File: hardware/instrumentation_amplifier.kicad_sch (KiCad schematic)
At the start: 7 parts, among them U3 MCP6N11-010, U4 MCP4542

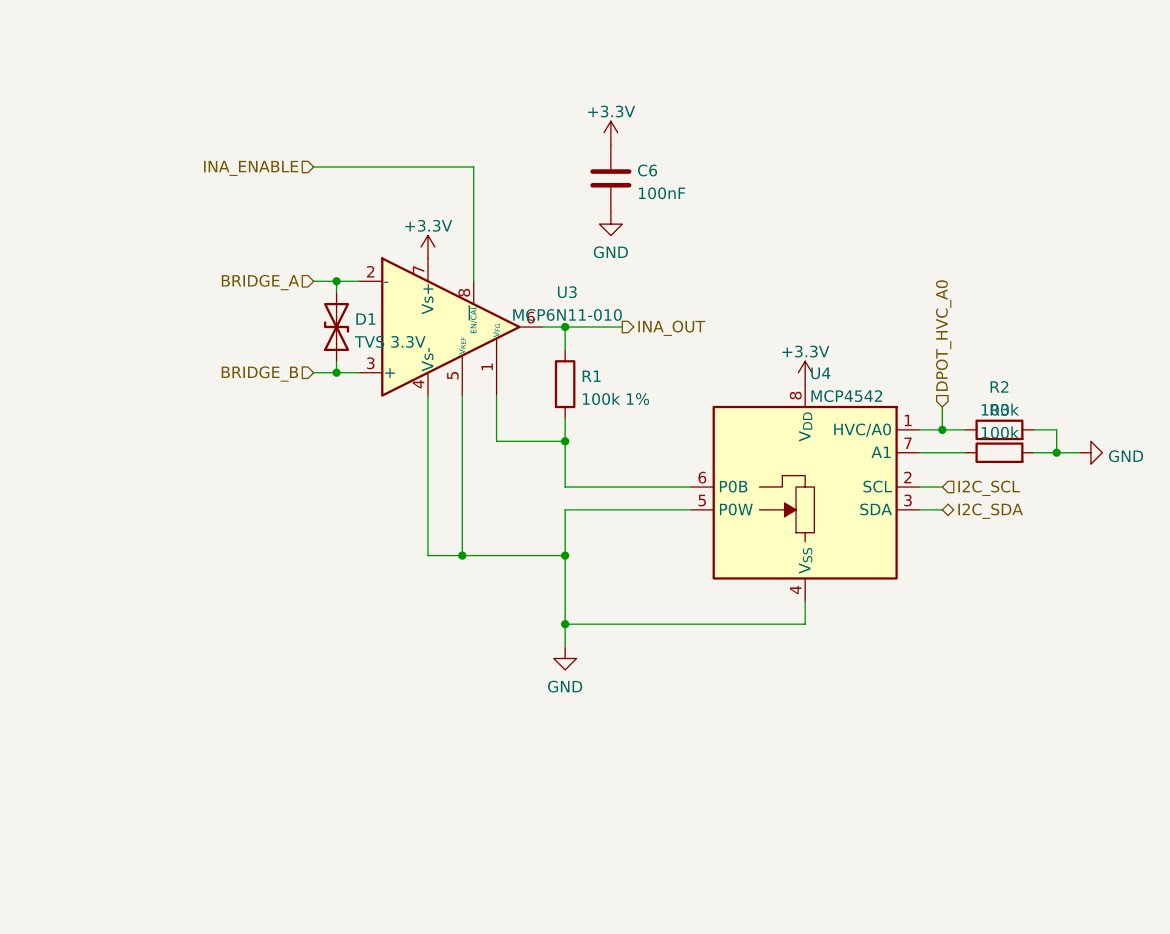
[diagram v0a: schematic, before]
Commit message: Updated schematic according to reference design
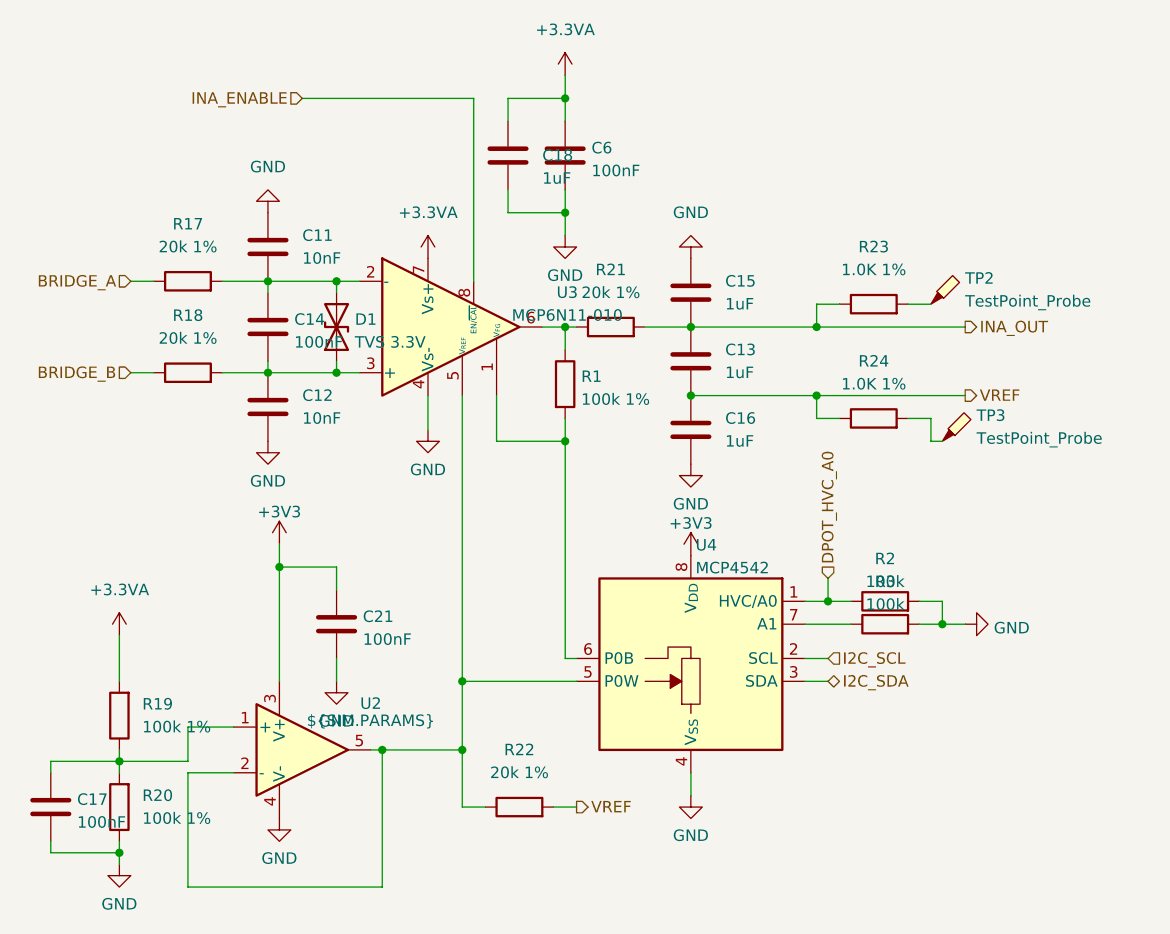
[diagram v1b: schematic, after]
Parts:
- added C11, C12: 10nF, Capacitor_SMD:C_0603_1608Metric_Pad1.08x0.95mm_HandSolder, symbol Device:C
- added C13, C15, C16, C18: 1uF, Capacitor_SMD:C_0603_1608Metric_Pad1.08x0.95mm_HandSolder, symbol Device:C
- added C14, C17, C21: 100nF, Capacitor_SMD:C_0603_1608Metric_Pad1.08x0.95mm_HandSolder, symbol Device:C
- added R17, R18, R21, R22: 20k 1%, Resistor_SMD:R_0603_1608Metric_Pad0.98x0.95mm_HandSolder, symbol Device:R
- added R19, R20: 100k 1%, Resistor_SMD:R_0603_1608Metric_Pad0.98x0.95mm_HandSolder, symbol Device:R
- added R23, R24: 1.0K 1%, Resistor_SMD:R_0603_1608Metric_Pad0.98x0.95mm_HandSolder, symbol Device:R
- added TP2, TP3: TestPoint_Probe, symbol Connector:TestPoint_Probe
- added U2: ${SIM.PARAMS}, symbol Simulation_SPICE:OPAMP
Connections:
- net +3V3: now also C21.1, U2.3 (V+); no longer C6.1, U3.7 (Vs+)
- net BRIDGE_A: now also R17.1; no longer D1.2 (A2), U3.2 (-)
- net BRIDGE_B: now also R18.1; no longer D1.1 (A1), U3.3 (+)
- net GND: now also C11.1, C12.2, C15.1, C16.2, C17.2, C18.2, C21.2, R20.1, U2.4 (V-); no longer U3.5 (V_{REF}), U4.5 (P0W)
- net INA_OUT: now also C13.1, C15.2, R21.2, R23.1; no longer R1.1, U3.6
- new net: R24.2, TP3.1
- new net: R1.1, R21.1, U3.6
- new net: C12.1, C14.2, D1.1 (A1), R18.2, U3.3 (+)
- new net: C17.1, R19.1, R20.2, U2.1 (+)
- new net: R22.1, U2.2 (-), U2.5, U3.5 (V_{REF}), U4.5 (P0W)
- new net: C11.2, C14.1, D1.2 (A2), R17.2, U3.2 (-)
- new net: R23.2, TP2.1
- new net +3.3VA: C18.1, C6.1, R19.2, U3.7 (Vs+)
- new net VREF: C13.2, C16.1, R22.2, R24.1
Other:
- moved on the sheet: C6, R2, R3, U4

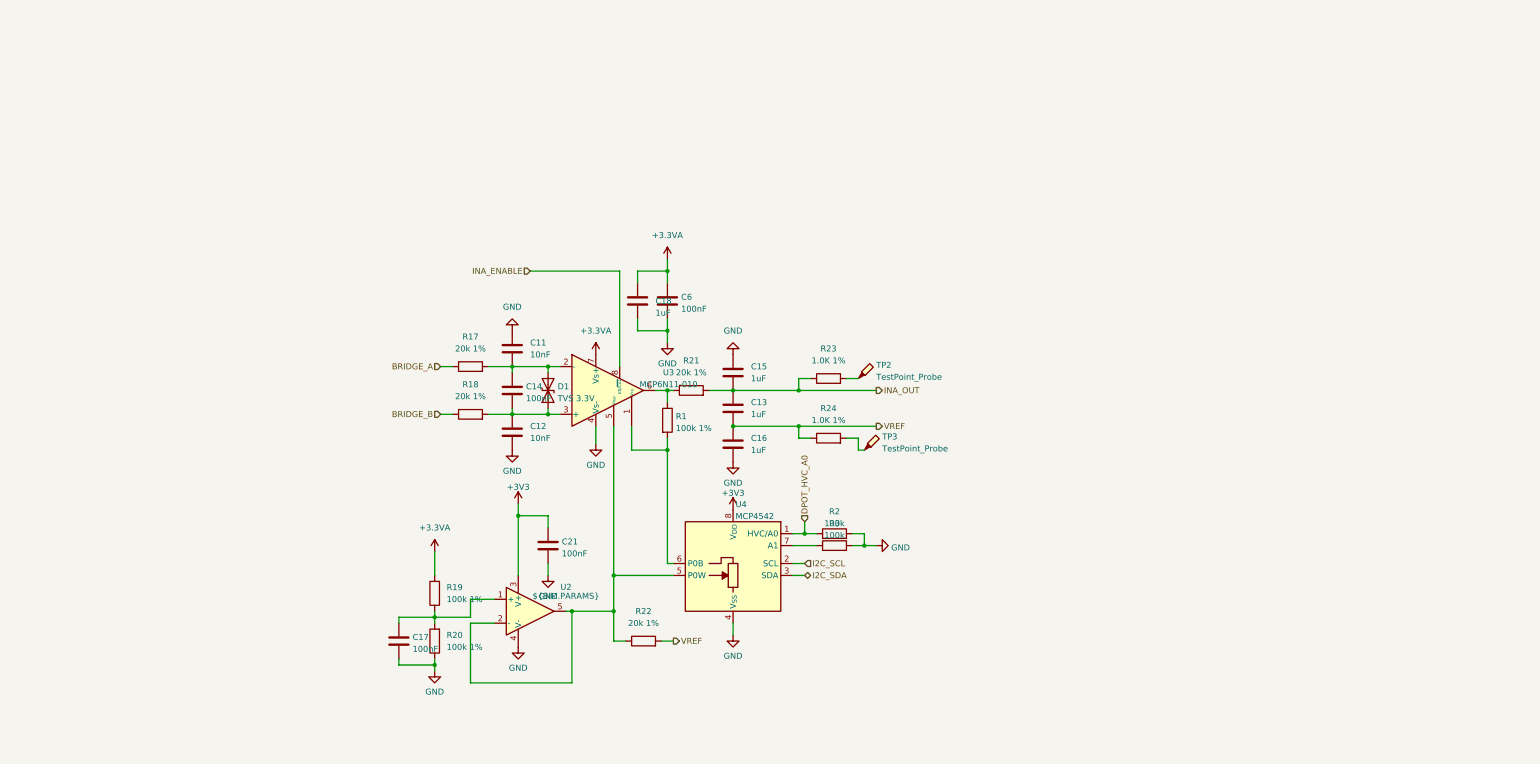
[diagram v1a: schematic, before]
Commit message: Include active filter, ext. ADC, changes to power supply
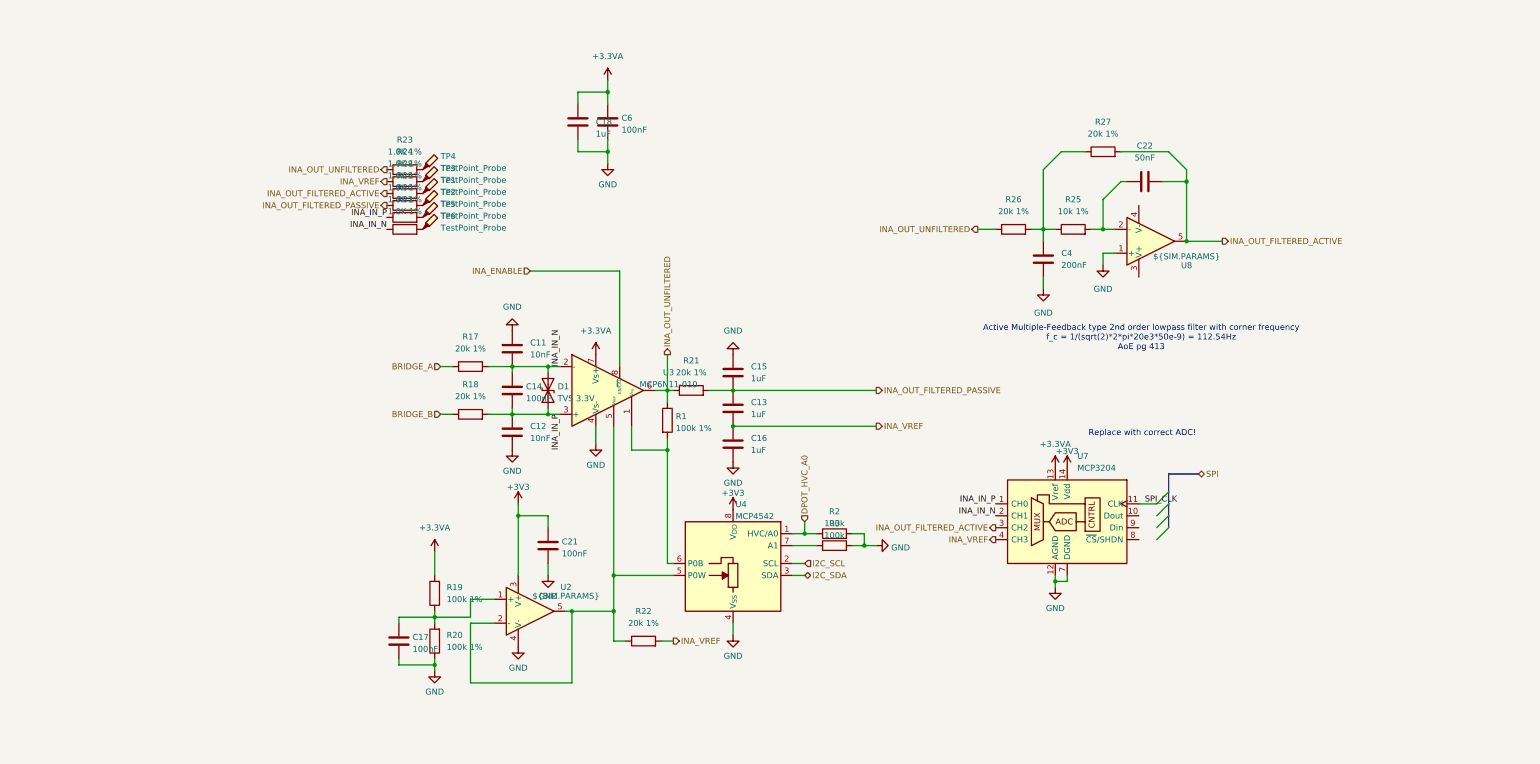
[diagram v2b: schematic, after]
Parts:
- added C22: 50nF, Capacitor_SMD:C_0603_1608Metric_Pad1.08x0.95mm_HandSolder, symbol Device:C
- added C4: 200nF, Capacitor_SMD:C_0603_1608Metric_Pad1.08x0.95mm_HandSolder, symbol Device:C
- added R25: 10k 1%, Resistor_SMD:R_0603_1608Metric_Pad0.98x0.95mm_HandSolder, symbol Device:R
- added R26, R27: 20k 1%, Resistor_SMD:R_0603_1608Metric_Pad0.98x0.95mm_HandSolder, symbol Device:R
- added R28, R29, R30, R31: 1.0K 1%, Resistor_SMD:R_0603_1608Metric_Pad0.98x0.95mm_HandSolder, symbol Device:R
- added TP1, TP4, TP5, TP6: TestPoint_Probe, symbol Connector:TestPoint_Probe
- added U7: MCP3204, symbol Analog_ADC:MCP3204
- added U8: ${SIM.PARAMS}, symbol Simulation_SPICE:OPAMP
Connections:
- net +3.3VA: now also U7.13 (Vref)
- net +3V3: now also U7.14 (Vdd)
- net GND: now also C4.2, U7.12 (AGND), U7.7 (DGND), U8.1 (+)
- net INA_OUT_UNFILTERED: now reaches R1.1, R21.1, U3.6
- net INA_OUT_UNFILTERED: now also R23.1, R26.1
- net INA_IN_P: now reaches C12.1, C14.2, D1.1 (A1), R18.2, U3.3 (+)
- net INA_IN_P: now also R30.1, U7.1 (CH0)
- net INA_IN_N: now reaches C11.2, C14.1, D1.2 (A2), R17.2, U3.2 (-)
- net INA_IN_N: now also R31.1, U7.2 (CH1)
- net at R23.2: now also TP4.1; no longer TP2.1
- net INA_OUT renamed INA_OUT_FILTERED_PASSIVE
- net INA_OUT_FILTERED_PASSIVE: now also R29.1; no longer R23.1
- net VREF renamed INA_VREF
- net INA_VREF: now also U7.4 (CH3)
- new net: R31.2, TP6.1
- new net: R28.2, TP1.1
- new net: C4.1, R25.1, R26.2, R27.1
- new net: R30.2, TP5.1
- new net: C22.1, R25.2, U8.2 (-)
- new net: R29.2, TP2.1
- new net INA_OUT_FILTERED_ACTIVE: C22.2, R27.2, R28.1, U7.3 (CH2), U8.5
- new net SPI_CLK: U7.11 (CLK)
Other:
- note added: "Active Multiple-Feedback type 2nd order lowpass filter with corner frequency f_c = 1/(sqrt(2)*2*pi*20e3*50e-9) = 112.54Hz AoE pg 413"
- note added: "Replace with correct ADC!"
- moved on the sheet: C18, C6, R23, R24, TP2, TP3

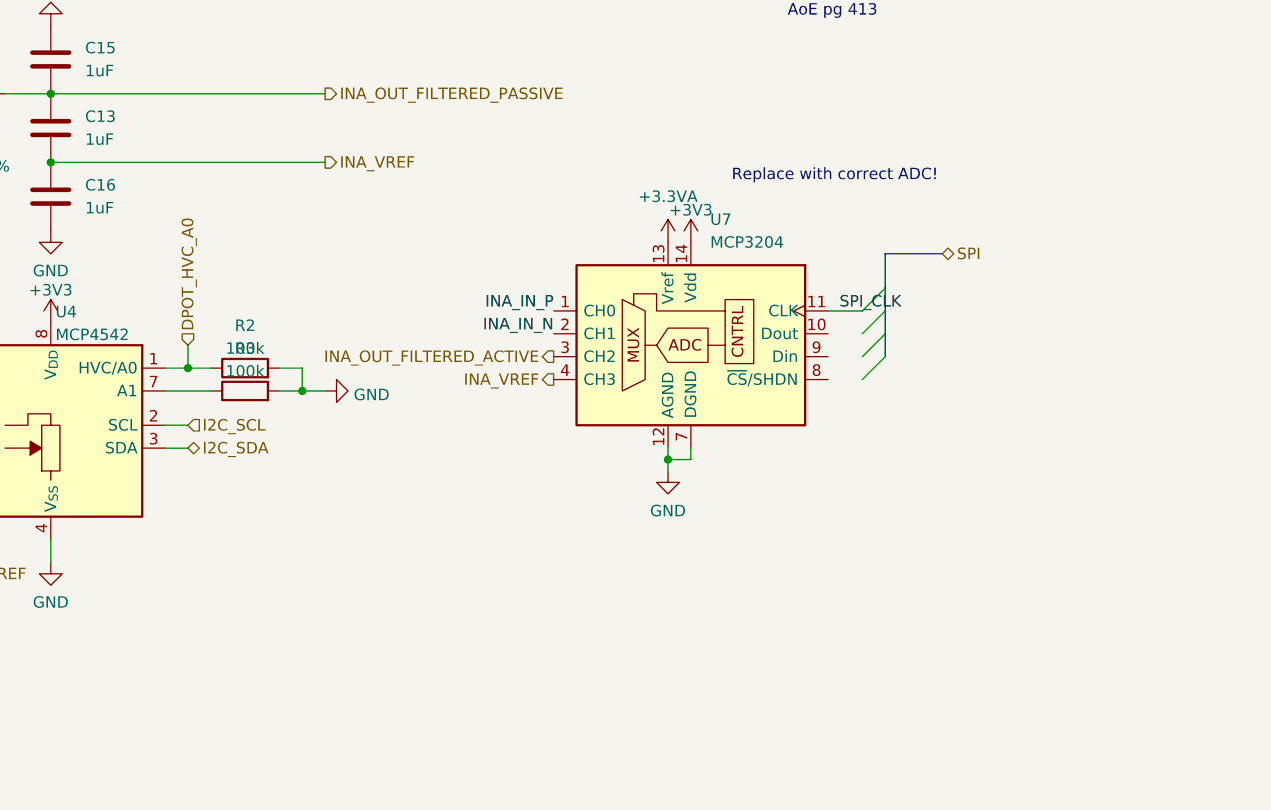
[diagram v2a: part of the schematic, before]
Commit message: Added correct symbol and libraries for ADC
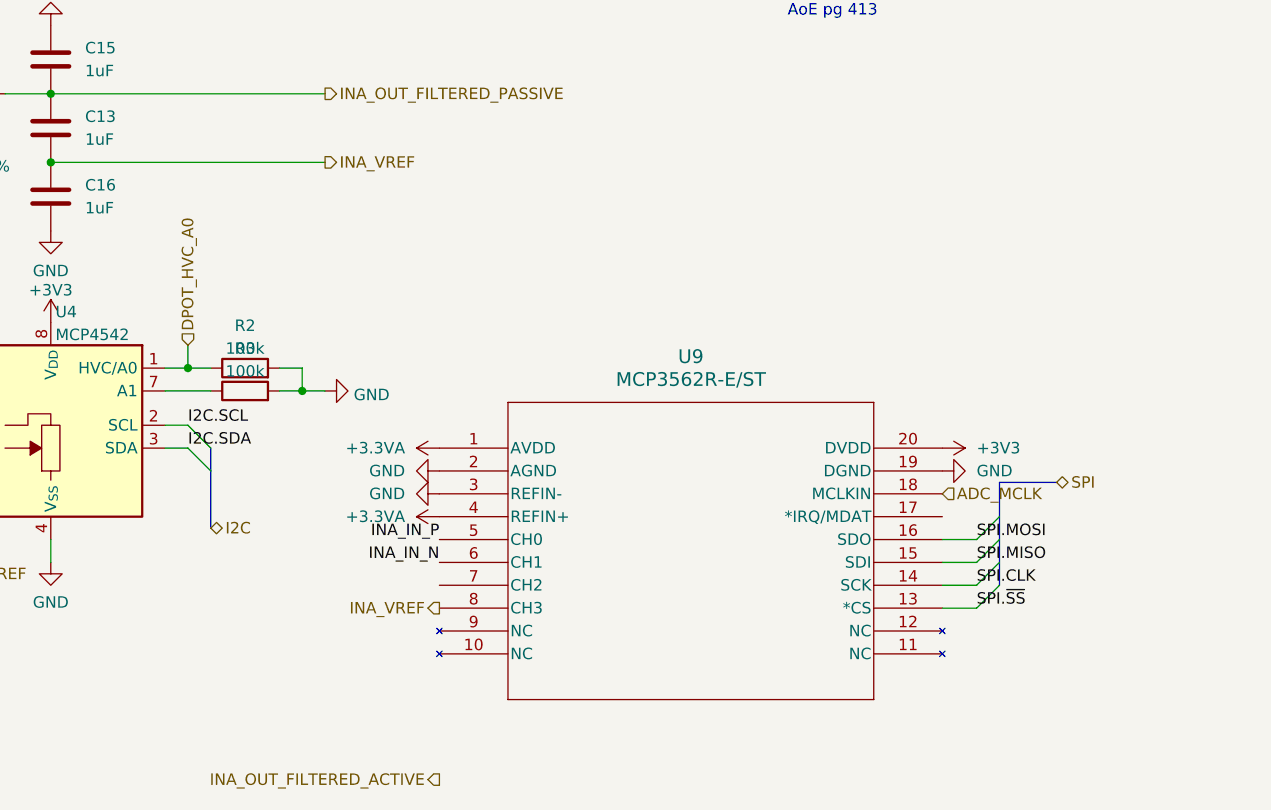
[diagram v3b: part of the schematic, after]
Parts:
- removed U7: MCP3204, symbol Analog_ADC:MCP3204
- added U9: MCP3562R-E/ST, Package_SO:TSSOP-20_4.4x6.5mm_P0.65mm, symbol 2025-11-03_20-40-54:MCP3562R-E_ST
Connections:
- net +3.3VA: now also U9.1 (AVDD), U9.4 (REFIN+)
- net +3V3: now also U9.20 (DVDD)
- net GND: now also U9.19 (DGND), U9.2 (AGND), U9.3 (REFIN-)
- net INA_IN_N: now also U9.6 (CH1)
- net INA_IN_P: now also U9.5 (CH0)
- net INA_VREF: now also U9.8 (CH3)
- net I2C_SCL renamed I2C.SCL
- net I2C_SDA renamed I2C.SDA
- new net ADC_MCLK: U9.18 (MCLKIN)
- new net SPI.CLK: U9.14 (SCK)
- new net SPI.MISO: U9.15 (SDI)
- new net SPI.MOSI: U9.16 (SDO)
- new net SPI.~{SS}: U9.13 (*CS)
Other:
- note removed: "Replace with correct ADC!"

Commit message: Regenerated reference designators, changed to rail-to-rail op-amps
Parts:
- removed U2, U8: ${SIM.PARAMS}, symbol Simulation_SPICE:OPAMP
- added C23: 100nF, Capacitor_SMD:C_0603_1608Metric_Pad1.08x0.95mm_HandSolder, symbol Device:C
- added U10, U9: MCP6001-OT, Package_TO_SOT_SMD:SOT-23-5, symbol Amplifier_Operational:MCP6001-OT
- C15: renamed from C4; value 200nF -> 220nF
- C16: renamed from C22; value 50nF -> 47nF
- renumbered C18 to C10, C6 to C11, C15 to C12, C16 to C14, C17 to C5, C11 to C6, C14 to C7, C12 to C8, C21 to C9, R23 to R1, R18 to R10, R22 to R11, R1 to R12, R21 to R13, R2 to R14, R3 to R15, R26 to R16, R25 to R17, R27 to R18, R24 to R2, R28 to R3, R29 to R4, R30 to R5, R31 to R6, R19 to R7, R20 to R8, R17 to R9, TP4 to TP1, TP3 to TP2, TP1 to TP3, TP2 to TP4, U9 to U5
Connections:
- net +3.3VA: now also C9.1, C23.1, U10.5 (V+), U9.5 (V+)
- net +3V3: no longer C9.1
- net GND: now also C23.2, U10.2 (V-), U9.2 (V-), U9.3 (+)
- net INA_OUT_FILTERED_ACTIVE: now also U5.7 (CH2), U9.1
- net at C5.1, R7.1, R8.2: now also U10.3 (+)
- net at R11.1, U3.5 (V_{REF}), U4.5 (P0W): now also U10.1, U10.4 (-)
- net at C16.1, R17.2: now also U9.4 (-)
- net ADC_IRQ: now reaches U5.17 (*IRQ/MDAT)
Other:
- note added: "Danger: Ideally do not use a quad op-amp with max output voltage 1V smaller than positive supply. Not good."
- moved on the sheet: C10, C11, C5, R7, R8

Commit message: Major changes to schematic
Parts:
- removed U5: MCP3562R-E/ST, Package_SO:TSSOP-20_4.4x6.5mm_P0.65mm, symbol 2025-11-03_20-40-54:MCP3562R-E_ST
- C10, C11, C12, C13, C14, C15, C16, C23, C5, C6, C7, C8, C9: footprint Capacitor_SMD:C_0603_1608Metric_Pad1.08x0.95mm_HandSolder -> Capacitor_SMD:C_0603_1608Metric
- D1: footprint Diode_SMD:D_SOD-323_HandSoldering -> Diode_SMD:D_SOD-323F
- R1, R10, R11, R12, R13, R14, R15, R16, R17, R18, R2, R3, R4, R5, R6, R7, R8, R9: footprint Resistor_SMD:R_0603_1608Metric_Pad0.98x0.95mm_HandSolder -> Resistor_SMD:R_0603_1608Metric
- TP1: value TestPoint_Probe -> TP_INA_OUT_UNFILTERED; footprint (none) -> TestPoint:TestPoint_Pad_D1.5mm
- TP2: value TestPoint_Probe -> TP_ADC_VREF; footprint (none) -> TestPoint:TestPoint_Pad_D1.5mm
- TP3: value TestPoint_Probe -> TP_INA_OUT_ACTIVE; footprint (none) -> TestPoint:TestPoint_Pad_D1.5mm
- TP4: value TestPoint_Probe -> TP_INA_OUT_FILTERED_PASSIVE; footprint (none) -> TestPoint:TestPoint_Pad_D1.5mm
- TP5: value TestPoint_Probe -> TP_INA_IN_P; footprint (none) -> TestPoint:TestPoint_Pad_D1.5mm
- TP6: value TestPoint_Probe -> TP_INA_IN_N; footprint (none) -> TestPoint:TestPoint_Pad_D1.5mm
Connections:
- net INA_VREF: now also R11.1, U10.1, U10.4 (-), U3.5 (V_{REF}), U4.5 (P0W); no longer C13.2, C14.1, R11.2, R2.1
- net I2C.SCL renamed SCL
- net I2C.SDA renamed SDA
- new net ADC_VREF: C13.2, C14.1, R11.2, R2.1
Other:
- note added: "Put a filter after the reference voltage opamp?"
- moved on the sheet: C10, C11, C15, C16, C23, C5, C9, R1, R16, R17, R18, R2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
